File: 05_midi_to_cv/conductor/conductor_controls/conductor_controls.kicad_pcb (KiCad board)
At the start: 2 copper layers, 26 x 100 mm, 23 parts, among them IC1 TLP2662, IC2 TLP2662, IC3 TLP2662, J4 to main board, J9 Conn_01x04_Socket

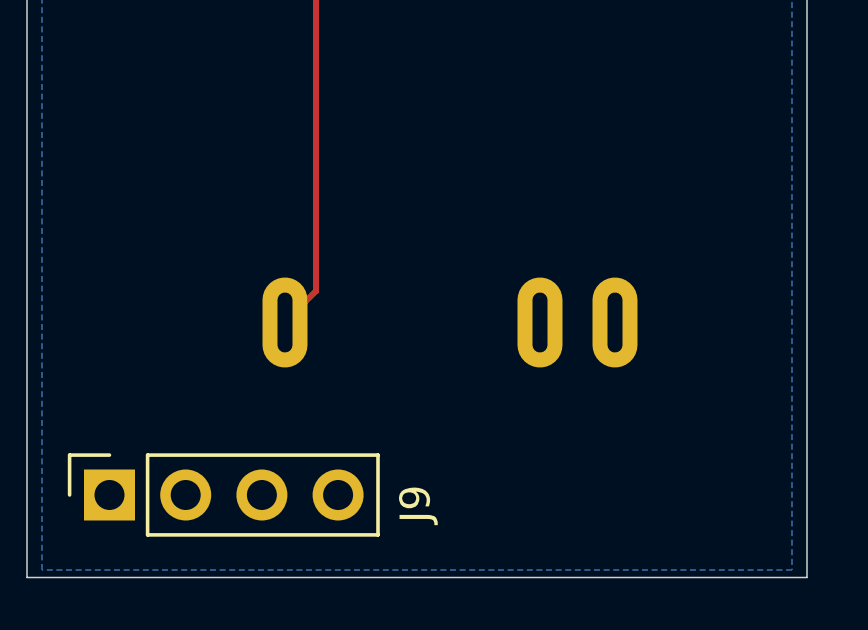
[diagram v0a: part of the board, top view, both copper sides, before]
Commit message: removed LED, first draft for panel
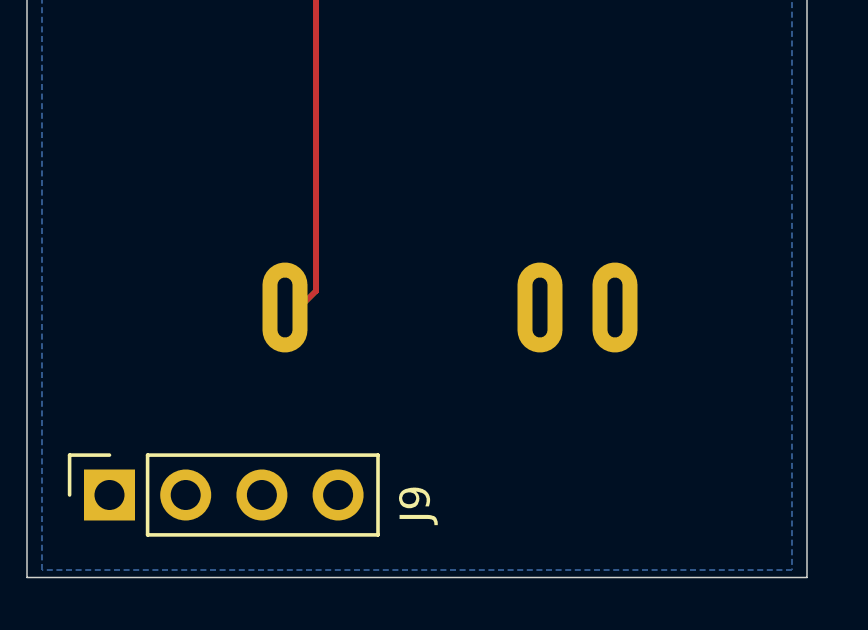
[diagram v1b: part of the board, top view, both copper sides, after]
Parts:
- moved J7 0.50 mm to (13.0, 91.0)
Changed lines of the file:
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@@
 	(footprint "cynthia:3.5mm thonk jack socket mono switched"
 		(layer "B.Cu")
-		(at 13 91.5 -90)
+		(at 13 91 -90)
 		(property "Reference" "J7"
 			(at -2.54 -8.382 90)

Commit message: 05 rev1
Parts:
- moved J5 1.00 mm to (13.0, 68.0)
- moved J7 1.00 mm to (13.0, 90.0)
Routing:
- net Net-(J7-PadT): track 35.2 -> 33.7 mm
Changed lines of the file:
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@@
 	(footprint "cynthia:3.5mm thonk jack socket mono switched"
 		(layer "B.Cu")
-		(at 13 91 -90)
+		(at 13 90 -90)
 		(property "Reference" "J7"
 			(at -2.54 -8.382 90)
@@
 	(footprint "cynthia:3.5mm thonk jack socket mono switched"
 		(layer "B.Cu")
-		(at 12.984 67 -90)
+		(at 13 68 -90)
 		(property "Reference" "J5"
 			(at -2.54 -8.382 90)
@@
 	)
 	(segment
+		(start 9.634 88.966)
+		(end 9.634 80.200926)
+		(width 0.2)
+		(layer "F.Cu")
+		(net "Net-(J7-PadT)")
+	)
+	(segment
+		(start 9.984 63.5)
+		(end 12.484 61)
+		(width 0.2)
+		(layer "F.Cu")
+		(net "Net-(J7-PadT)")
+	)
+	(segment
+		(start 8.584 90.016)
+		(end 9.634 88.966)
+		(width 0.2)
+		(layer "F.Cu")
+		(net "Net-(J7-PadT)")
+	)
+	(segment
+		(start 9.65 80.184926)
+		(end 9.65 72.666)
+		(width 0.2)
+		(layer "F.Cu")
+		(net "Net-(J7-PadT)")
+	)
+	(segment
+		(start 7 64.984)
+		(end 8.484 63.5)
+		(width 0.2)
+		(layer "F.Cu")
+		(net "Net-(J7-PadT)")
+	)
+	(segment
+		(start 8.484 63.5)
+		(end 9.984 63.5)
+		(width 0.2)
+		(layer "F.Cu")
+		(net "Net-(J7-PadT)")
+	)
+	(segment
+		(start 9.634 80.200926)
+		(end 9.65 80.184926)
+		(width 0.2)
+		(layer "F.Cu")
+		(net "Net-(J7-PadT)")
+	)
+	(segment
+		(start 7 70.016)
+		(end 7 64.984)
+		(width 0.2)
+		(layer "F.Cu")
+		(net "Net-(J7-PadT)")
+	)
+	(segment
 		(start 9.65 72.666)
 		(end 7 70.016)
 		(width 0.2)
 		(layer "F.Cu")
-		(net "Net-(J7-PadT)")
-	)
-	(segment
-		(start 8.584 91.5)
-		(end 9.634 90.45)
-		(width 0.2)
-		(layer "F.Cu")
-		(net "Net-(J7-PadT)")
-	)
-	(segment
-		(start 9.65 80.184926)
-		(end 9.65 72.666)
-		(width 0.2)
-		(layer "F.Cu")
-		(net "Net-(J7-PadT)")
-	)
-	(segment
-		(start 7 70.016)
-		(end 7 64.984)
-		(width 0.2)
-		(layer "F.Cu")
-		(net "Net-(J7-PadT)")
-	)
-	(segment
-		(start 7 64.984)
-		(end 8.484 63.5)
-		(width 0.2)
-		(layer "F.Cu")
-		(net "Net-(J7-PadT)")
-	)
-	(segment
-		(start 8.484 63.5)
-		(end 9.984 63.5)
-		(width 0.2)
-		(layer "F.Cu")
-		(net "Net-(J7-PadT)")
-	)
-	(segment
-		(start 9.984 63.5)
-		(end 12.484 61)
-		(width 0.2)
-		(layer "F.Cu")
-		(net "Net-(J7-PadT)")
-	)
-	(segment
-		(start 9.634 80.200926)
-		(end 9.65 80.184926)
-		(width 0.2)
-		(layer "F.Cu")
-		(net "Net-(J7-PadT)")
-	)
-	(segment
-		(start 9.634 90.45)
-		(end 9.634 80.200926)
-		(width 0.2)
-		(layer "F.Cu")

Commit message: worked on issues after building #05
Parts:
- IC1, IC2, IC3: footprint Package_DIP:SMDIP-8_W7.62mm -> cynthia:SMDIP-8_W7.62mm_hand_solder
- moved IC2 90.3 mm to (82.2, 77.0)
- moved C1 90.1 mm to (97.5, 53.5)
- moved C2 90.1 mm to (85.5, 70.5)
- moved C3 90.1 mm to (97.5, 87.5)
- moved IC1 90.1 mm to (94.0, 60.0)
- moved IC3 90.1 mm to (94.2, 94.0)
- moved J1 90.1 mm to (82.5, 60.0)
- moved J2 90.1 mm to (93.5, 77.0)
- moved J3 90.1 mm to (82.5, 94.0)
- moved J4 90.1 mm to (80.2, 106.0)
- moved J5 90.1 mm to (88.0, 118.0)
- moved J6 90.1 mm to (88.0, 129.0)
- moved J7 90.1 mm to (88.0, 140.0)
- moved J9 90.1 mm to (77.8, 147.2)
- moved R2 90.1 mm to (81.8, 83.5)
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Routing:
- net +3.3V: track 141.5 -> 144.8 mm
- net Net-(IC1-Pad2): track 12.2 -> 13.6 mm
- net Net-(IC2-Pad2): track 30.2 -> 31.6 mm
- net Net-(IC3-Pad2): track 12.1 -> 13.3 mm
- net MIDI_2: track 59.4 -> 60.4 mm
- net Net-(J2-PadR): track 11.5 -> 12.0 mm
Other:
- board text added: "#05: Conductor: Control Board Rev. 2 2026 Benjamin Murauer"
